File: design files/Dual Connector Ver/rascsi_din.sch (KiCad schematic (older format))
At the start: 24 parts, among them J1 Raspberry_Pi_2_3, J2 DB25_Female, J3 Conn_02x25_Odd_Even, U1 SN74LS641-1C, U2 SN74LS641-1C, U3 SN74LS641-1C, U4 SN74LS641-1C

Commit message: Corrected pinout to match original RaSCSI design.
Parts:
- removed D2, D3, D4, D5: LED_Small, LED_SMD:LED_0805_2012Metric, symbol Device:LED_Small
- removed FUSE1A1: R-US_0204_7, rascsi_din:0204_7, symbol rascsi_din-eagle-import:R-US_0204_7
- removed J1: Raspberry_Pi_2_3, Connector_PinSocket_2.54mm:PinSocket_2x20_P2.54mm_Vertical, symbol Connector:Raspberry_Pi_2_3
- removed J2: DB25_Female, Connector_Dsub:DSUB-25_Female_Horizontal_P2.77x2.84mm_EdgePinOffset4.94mm_Housed_MountingHolesOffset7.48mm, symbol Connector:DB25_Female
- removed J3: Conn_02x25_Odd_Even, Connector_PinHeader_2.54mm:PinHeader_2x25_P2.54mm_Vertical_SMD, symbol Connector_Generic:Conn_02x25_Odd_Even
- removed R1, R2, R3, R4: 10k, Resistor_SMD:R_0805_2012Metric, symbol Device:R_Small
- removed RN1, RN2: 10k, Resistor_THT:R_Array_SIP10, symbol Device:R_Network09
- removed RN3, RN5: 220, Resistor_THT:R_Array_SIP10, symbol Device:R_Network09
- removed RN4, RN6: 330, Resistor_THT:R_Array_SIP10, symbol Device:R_Network09
- added FUSE1A: R-US_0204_7, rascsi_din:0204_7, symbol rascsi_din-eagle-import:R-US_0204_7
- added JP1: PINHD-1X2, rascsi_din:1X02, symbol rascsi_din-eagle-import:PINHD-1X2
- added RN1, RN2: 10k, rascsi_din:RN-10, symbol rascsi_din-eagle-import:RN09
- added RN3, RN5: 220, rascsi_din:RN-10, symbol rascsi_din-eagle-import:RN09
- added RN4, RN6: 330, rascsi_din:RN-10, symbol rascsi_din-eagle-import:RN09
- added U$1: ZERO, rascsi_din:ZERO, symbol rascsi_din-eagle-import:ZERO
- added X1: F25?SHP, rascsi_din:F25HP, symbol rascsi_din-eagle-import:F25?SHP
- renumbered U$1 to U$2, U3 to U11, U4 to U22, U1 to U33, U2 to U44
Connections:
- net labels added: ACK, ATN, BSY, C-CD, C-IO, CD, D0, D1, D2, D3, D4, D5, D6, D7, DP, IO, MSG, REQ, RST, SEL
- net labels removed: C-C_D, C-I_O, DBG_LED, PI-ACK, PI-ATN, PI-BSY, PI-C_D, PI-D0, PI-D1, PI-D2, PI-D3, PI-D4, PI-D5, PI-D6, PI-D7, PI-DP, PI-I_O, PI-MSG, PI-REQ, PI-RST, PI-SEL
- wire segments 163 -> 417
- no-connect marks 11 -> 0
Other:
- note added: "3 4 etc"
- note added: "Goes 1 2"
- note added: "Note the original has ATOB for DIR for some reason...\nAnd G is active low, but this is taken care of in the design"
- note removed: "Activity, Debug and Power LEDs"
- note removed: "Change direction based upon PI-I_O"
- note removed: "DB-25 SCSI Connector"
- note removed: "DIR = +5v\nA is input, B is output"
- note removed: "DIR = GND\nB is input, A is output"
- note removed: "Note the original RaSCSI design calls the DIR pin "ATOB"\nEnable Input ("G") is active low, so always grounded."
- note removed: "ONLY THE DB-25 OR RIBBON CABLE SHOULD BE USED!!\nDO NOT USE BOTH AT THE SAME TIME!"
- note removed: "Pull-up resistors for Raspberry Pi 3.3v Signals"
- note removed: "Raspberry Pi Connector"
- note removed: "SCSI Bus Transceivers"
- note removed: "SCSI Ribbon Cable"
- note removed: "SCSI Termination Resistors"
- note removed: "Terminating Resistor Power"
- note removed: "This card include bus transceiver logic to allow a Raspberry \nPi to connect to a vintage Macintosh SCSI port. (It may \nwork with other systems as well)\n\nThis design is based upon fran-cap's design\nhttps://github.com/fran-cap/RASCSI-68kmlaver\n... which was based on the original Gimmons design:\nhttp://retropc.net/gimons/rascsi/\n\nThank you to everyone who has worked on this project!!"
- note removed: "fran-cap's Logo"

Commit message: Restored the correct version of the schematic & added notes to fix the PI-ACT signal. Also adding the gerber files.
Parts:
- removed FUSE1A: R-US_0204_7, rascsi_din:0204_7, symbol rascsi_din-eagle-import:R-US_0204_7
- removed JP1: PINHD-1X2, rascsi_din:1X02, symbol rascsi_din-eagle-import:PINHD-1X2
- removed RN1, RN2: 10k, rascsi_din:RN-10, symbol rascsi_din-eagle-import:RN09
- removed RN3, RN5: 220, rascsi_din:RN-10, symbol rascsi_din-eagle-import:RN09
- removed RN4, RN6: 330, rascsi_din:RN-10, symbol rascsi_din-eagle-import:RN09
- removed U$1: ZERO, rascsi_din:ZERO, symbol rascsi_din-eagle-import:ZERO
- removed X1: F25?SHP, rascsi_din:F25HP, symbol rascsi_din-eagle-import:F25?SHP
- added D2, D3, D4, D5: LED_Small, LED_SMD:LED_0805_2012Metric, symbol Device:LED_Small
- added FUSE1A1: R-US_0204_7, rascsi_din:0204_7, symbol rascsi_din-eagle-import:R-US_0204_7
- added H1: Hole1, MountingHole:MountingHole_2.7mm_M2.5_Pad_Via, symbol Mechanical:MountingHole_Pad
- added H2: Hole2, MountingHole:MountingHole_2.7mm_M2.5_Pad_Via, symbol Mechanical:MountingHole_Pad
- added H3: Hole3, MountingHole:MountingHole_2.7mm_M2.5_Pad_Via, symbol Mechanical:MountingHole_Pad
- added H4: Hole5, MountingHole:MountingHole_2.7mm_M2.5_Pad_Via, symbol Mechanical:MountingHole_Pad
- added H5: Hole4, MountingHole:MountingHole_2.7mm_M2.5_Pad_Via, symbol Mechanical:MountingHole_Pad
- added H6: Hole6, MountingHole:MountingHole_2.7mm_M2.5_Pad_Via, symbol Mechanical:MountingHole_Pad
- added J1: Raspberry_Pi_2_3, Connector_PinSocket_2.54mm:PinSocket_2x20_P2.54mm_Vertical, symbol Connector:Raspberry_Pi_2_3
- added J2: DLS3XS6AK44X, DLS3XS6AK44X, symbol Library_Loader_Parts:DLS3XS6AK44X
- added J3: Conn_02x25_Odd_Even, Connector_PinHeader_2.54mm:PinHeader_2x25_P2.54mm_Vertical_SMD, symbol Connector_Generic:Conn_02x25_Odd_Even
- added J4: I2C Pinout, Connector_PinSocket_2.54mm:PinSocket_1x05_P2.54mm_Vertical, symbol Connector:Conn_01x05_Male
- added JP1: Term_Enable_GND, Connector_PinSocket_2.54mm:PinSocket_1x02_P2.54mm_Vertical, symbol Device:Jumper_NC_Small
- added JP2: Term_Enable_5v, Connector_PinSocket_2.54mm:PinSocket_1x02_P2.54mm_Vertical, symbol Device:Jumper_NC_Small
- added L1: Mac, rascsi_din:mac_happy_small, symbol rascsi_din-eagle-import:LOGO
- added L2: Dogcow, rascsi_din:dogcow, symbol rascsi_din-eagle-import:LOGO
- added L3: Mac2, rascsi_din:mac_happy_small, symbol rascsi_din-eagle-import:LOGO
- added L4: Dogcow2, rascsi_din:dogcow, symbol rascsi_din-eagle-import:LOGO
- added L5, L7: Raspberry Pi, rascsi_din:pi_logo, symbol rascsi_din-eagle-import:LOGO
- added L6: Mac Trashcan, rascsi_din:mac_trashcan, symbol rascsi_din-eagle-import:LOGO
- added R1, R2, R4: 44, Resistor_SMD:R_0805_2012Metric, symbol Device:R_Small
- added R3: 112, Resistor_SMD:R_0805_2012Metric, symbol Device:R_Small
- added RN1, RN2: 10k, Resistor_THT:R_Array_SIP10, symbol Device:R_Network09
- added RN3, RN5: 220, Resistor_THT:R_Array_SIP10, symbol Device:R_Network09
- added RN4, RN6: 330, Resistor_THT:R_Array_SIP10, symbol Device:R_Network09
- renumbered U$2 to U$1, U33 to U1, U44 to U2, U11 to U3, U22 to U4
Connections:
- net labels added: C-C_D, C-I_O, DBG_LED, PI-ACK, PI-ATN, PI-BSY, PI-C_D, PI-D0, PI-D1, PI-D2, PI-D3, PI-D4, PI-D5, PI-D6, PI-D7, PI-DP, PI-I_O, PI-MSG, PI-REQ, PI-RST, PI-SEL, PI_SCL, PI_SDA
- net labels removed: ACK, ATN, BSY, C-CD, C-IO, CD, D0, D1, D2, D3, D4, D5, D6, D7, DP, IO, MSG, REQ, RST, SEL
- wire segments 417 -> 167
- no-connect marks 0 -> 9
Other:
- note added: "Activity, Debug and Power LEDs"
- note added: "Change direction based upon PI-I_O"
- note added: "DB-25 SCSI Connector"
- note added: "DIR = +5v\nA is input, B is output"
- note added: "DIR = GND\nB is input, A is output"
- note added: "Images"
- note added: "Jumper to enable or\ndisable SCSI \ntermination"
- note added: "Mounting Holes"
- note added: "Note the original RaSCSI design calls the DIR pin "ATOB"\nEnable Input ("G") is active low, so always grounded."
- note added: "ONLY THE DB-25 OR RIBBON CABLE SHOULD BE USED!!\nDO NOT USE BOTH AT THE SAME TIME!"
- note added: "Pull-up resistors for Raspberry Pi 3.3v Signals"
- note added: "Raspberry Pi Connector"
- note added: "SCSI Bus Transceivers"
- note added: "SCSI Ribbon Cable"
- note added: "SCSI Termination Resistors"
- note added: "THIS IS AN ERROR!!!\n"
- note added: "Terminating Resistor Power"
- note added: "This card include bus transceiver logic to allow a Raspberry \nPi to connect to a vintage Macintosh SCSI port. (It may \nwork with other systems as well)\n\nThis design is based upon fran-cap's design\nhttps://github.com/fran-cap/RASCSI-68kmlaver\n... which was based on the original Gimmons design:\nhttp://retropc.net/gimons/rascsi/\n\nThank you to everyone who has worked on this project!!"
- note added: "This should be PI-ACT. To correct this, cut \nthe trace to pin 1 of U3, and run a jumper \nwire to Pin 7 of the Raspberry Pi GPIO header."
- note removed: "3 4 etc"
- note removed: "Goes 1 2"
- note removed: "Note the original has ATOB for DIR for some reason...\nAnd G is active low, but this is taken care of in the design"

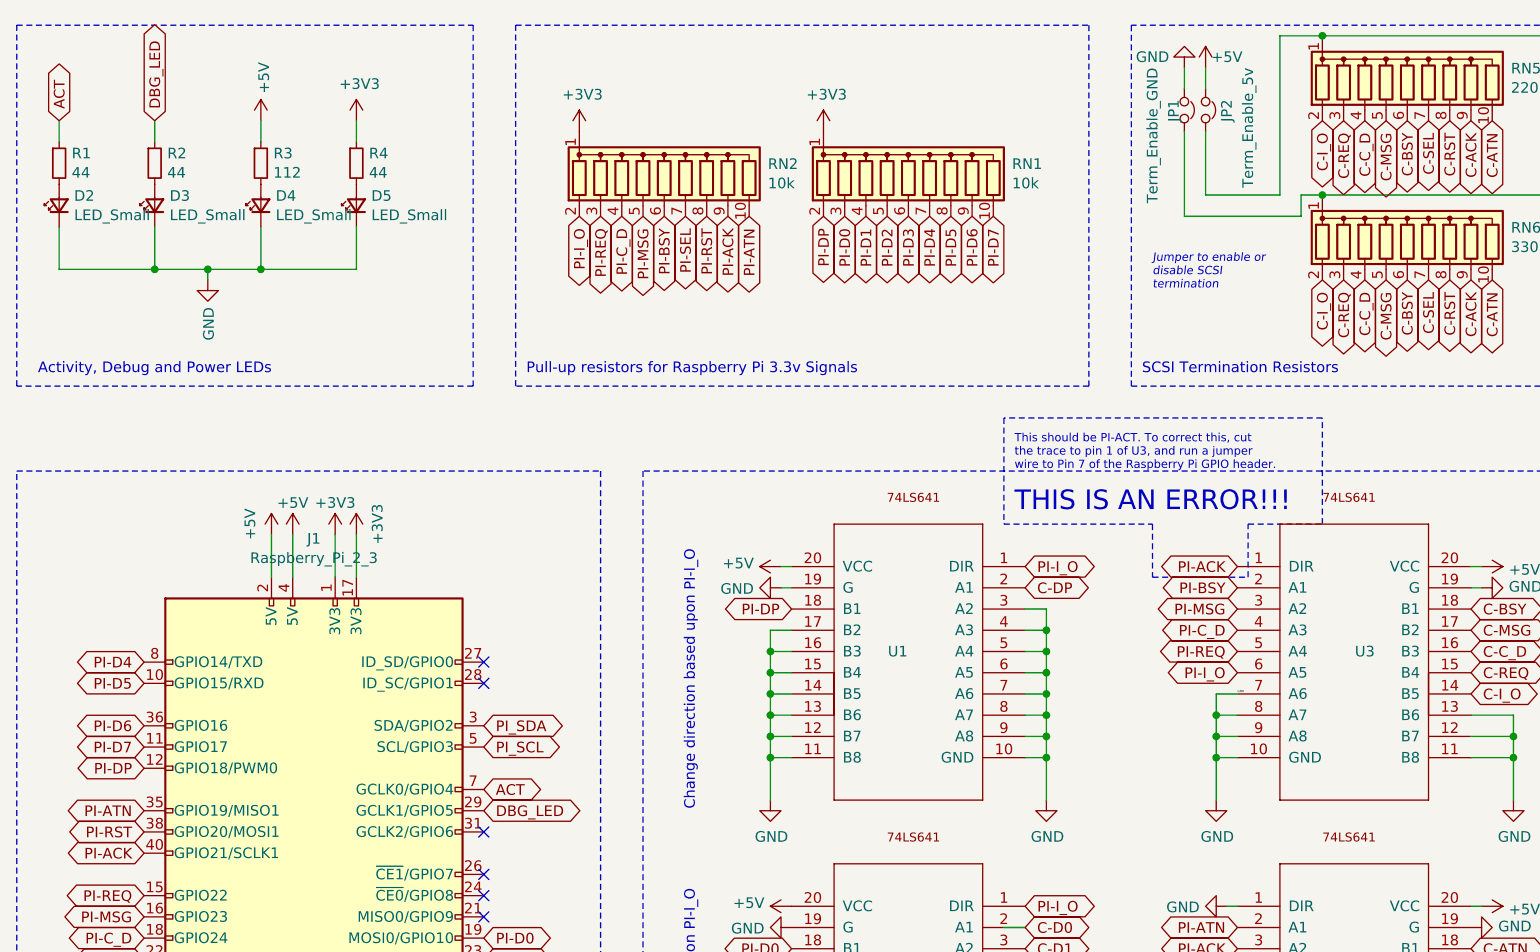
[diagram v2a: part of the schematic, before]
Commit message: Corrected ACT signal line
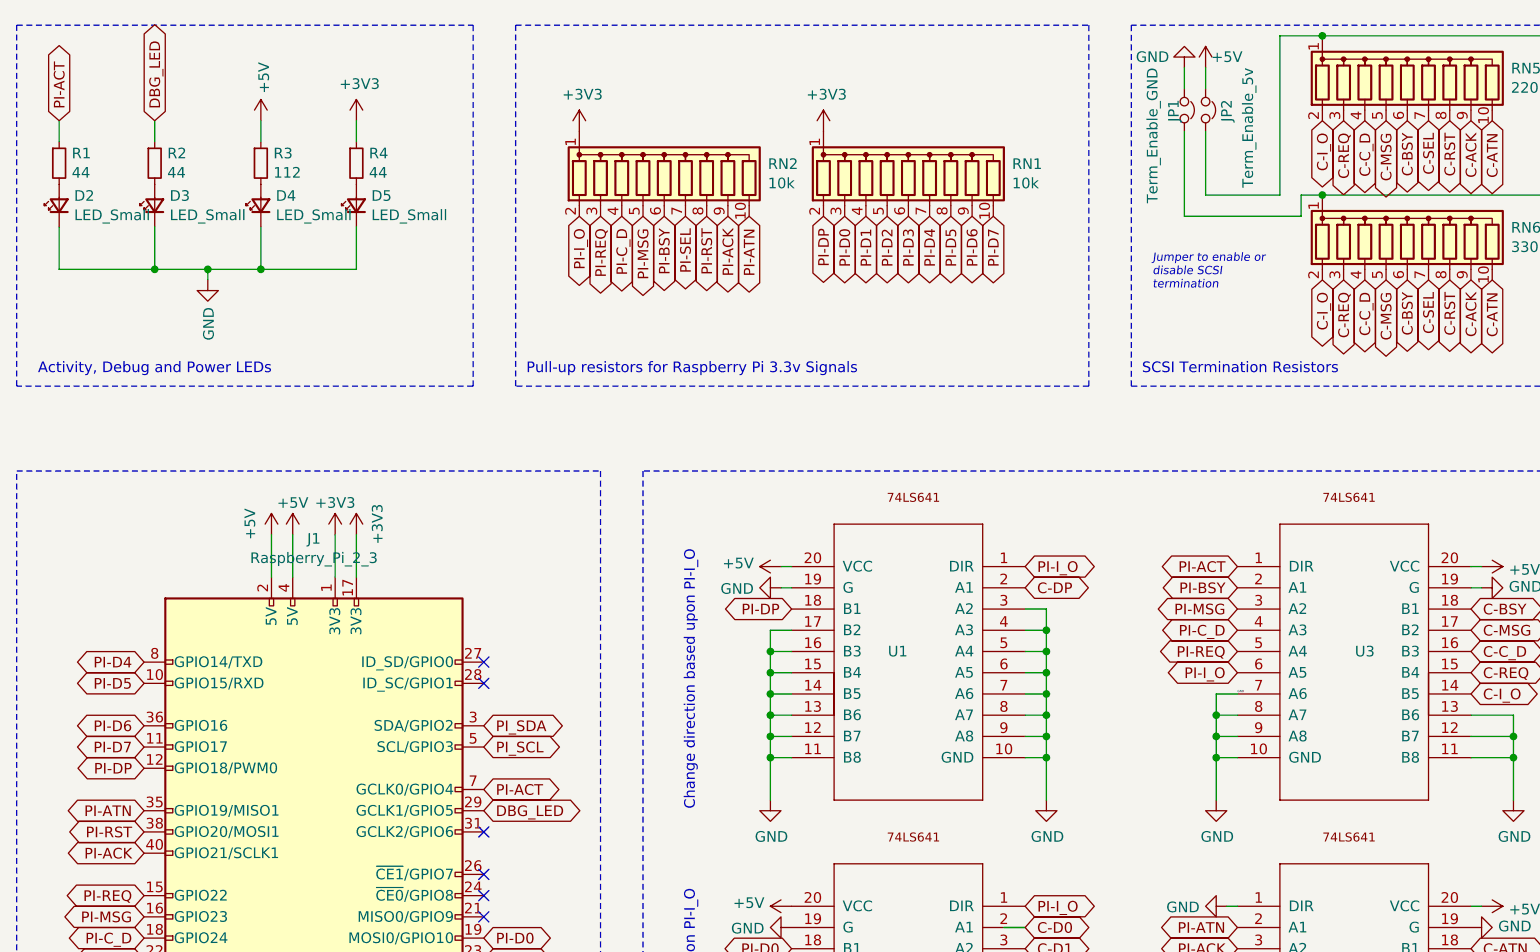
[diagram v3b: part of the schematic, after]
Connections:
- net labels added: PI-ACT
- net labels removed: ACT
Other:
- note removed: "THIS IS AN ERROR!!!\n"
- note removed: "This should be PI-ACT. To correct this, cut \nthe trace to pin 1 of U3, and run a jumper \nwire to Pin 7 of the Raspberry Pi GPIO header."
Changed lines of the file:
@@
-$EndComp
-$Comp
-L power:+5V #PWR028
-U 1 1 6072B611
-P 6150 750
-F 0 "#PWR028" H 6150 600 50  0001 C CNN
-F 1 "+5V" H 6250 800 50  0000 C CNN
-F 2 "" H 6150 750 50  0001 C CNN
-F 3 "" H 6150 750 50  0001 C CNN
-	1    6150 750
-	1    0    0    -1
 $EndComp
 $Comp
@@
 	1    7100 1550
 	1    0    0    -1
-$EndComp
-$Comp
-L power:GND #PWR026
-U 1 1 6072B62D
-P 6050 750
-F 0 "#PWR026" H 6050 500 50  0001 C CNN
-F 1 "GND" H 6200 700 50  0000 C CNN
-F 2 "" H 6050 750 50  0001 C CNN
-F 3 "" H 6050 750 50  0001 C CNN
-	1    6050 750
-	-1   0    0    1
 $EndComp
 Text GLabel 7400 3600 2    50   BiDi ~ 0
@@
 PI-ATN
 Text GLabel 6300 3100 0    50   BiDi ~ 0
-PI-ACK
+PI-ACT
 Text GLabel 6300 5000 0    50   BiDi ~ 0
 PI-RST
@@
 PI-DP
 Text GLabel 750  1000 1    50   BiDi ~ 0
-ACT
+PI-ACT
 $Comp
 L power:GND #PWR08
@@
 PI-SEL
 Text GLabel 2750 4150 2    50   BiDi ~ 0
-ACT
+PI-ACT
 $Comp
 L power:+5V #PWR01
@@
 $EndComp
 Connection ~ 3300 7600
-$Comp
-L Library_Loader_Parts:DLS3XS6AK44X J2
-U 1 1 5F429403
-P 9200 4650
-F 0 "J2" H 11044 4696 50  0000 L CNN
-F 1 "DLS3XS6AK44X" V 10850 3950 50  0000 L CNN
-F 2 "DLS3XS6AK44X" H 10850 4950 50  0001 L CNN
-F 3 "https://componentsearchengine.com/Datasheets/1/DLS3XS6AK44X.pdf" H 10850 4850 50  0001 L CNN
-F 4 "D-Sub Standard Connectors 25P F R/A .370 4-40 C/W HEX" H 10850 4750 50  0001 L CNN "Description"
-F 5 "12.5" H 10850 4650 50  0001 L CNN "Height"
-F 6 "706-DLS3XS6AK44X" H 10850 4550 50  0001 L CNN "Mouser Part Number"
-F 7 "https://www.mouser.com/Search/Refine.aspx?Keyword=706-DLS3XS6AK44X" H 10850 4450 50  0001 L CNN "Mouser Price/Stock"
-F 8 "CONEC" H 10850 4350 50  0001 L CNN "Manufacturer_Name"
-F 9 "DLS3XS6AK44X" H 10850 4250 50  0001 L CNN "Manufacturer_Part_Number"
-	1    9200 4650
-	0    -1   -1   0
-$EndComp
 Text GLabel 8700 3850 0    50   BiDi ~ 0
 C-D0
@@
 Mounting Holes
 $Comp
-L power:+5V #PWR048
-U 1 1 5F0B94FB
-P 2950 6250
-F 0 "#PWR048" H 2950 6100 50  0001 C CNN
-F 1 "+5V" V 2950 6450 50  0000 C CNN
-F 2 "" H 2950 6250 50  0001 C CNN
-F 3 "" H 2950 6250 50  0001 C CNN
-	1    2950 6250
-	0    -1   -1   0
-$EndComp
-$Comp
 L power:GND #PWR047
 U 1 1 5F0B9E0E
@@
 Text GLabel 2950 5950 0    50   BiDi ~ 0
 PI_SCL
+Wire Notes Line
+	3300 5700 2550 5700
+Wire Notes Line
+	2550 5700 2550 6400
+NoConn ~ 2750 4750
+NoConn ~ 2750 4650
+NoConn ~ 2750 4550
+NoConn ~ 2750 4350
+NoConn ~ 2750 3550
+NoConn ~ 2750 3650
+Wire Notes Line
+	5800 2250 8900 2250
+Wire Wire Line
+	6700 600  7800 600
+Connection ~ 6700 600
+Wire Wire Line
+	6600 1350 6700 1350
+Wire Wire Line
+	7800 1350 6700 1350
+Connection ~ 6700 1350
+$Comp
+L rascsi_din-eagle-import:LOGO L7
+U 1 1 5F2D2B3B
+P 9050 6300
+F 0 "L7" H 8900 6300 50  0000 R CNN
+F 1 "Raspberry Pi" H 8950 6350 50  0000 R CNN
+F 2 "rascsi_din:pi_logo" H 9050 6300 50  0001 C CNN
+F 3 "" H 9050 6300 50  0001 C CNN
+	1    9050 6300
+	-1   0    0    1
+$EndComp
+$Comp
+L rascsi_din-eagle-import:LOGO L5
+U 1 1 5EFCDD94
+P 9550 5950
+F 0 "L5" H 9350 5950 50  0000 R CNN
+F 1 "Raspberry Pi" H 9400 6000 50  0000 R CNN
+F 2 "rascsi_din:pi_logo" H 9550 5950 50  0001 C CNN
+F 3 "" H 9550 5950 50  0001 C CNN
+	1    9550 5950
+	-1   0    0    1
+$EndComp
+$Comp
+L power:+5V #PWR048
+U 1 1 5F0B94FB
+P 2950 6250
+F 0 "#PWR048" H 2950 6100 50  0001 C CNN
+F 1 "+5V" V 2950 6450 50  0000 C CNN
+F 2 "" H 2950 6250 50  0001 C CNN
+F 3 "" H 2950 6250 50  0001 C CNN
+	1    2950 6250
+	0    -1   -1   0
+$EndComp
 $Comp
 L Connector:Conn_01x05_Male J4
@@
 	-1   0    0    1
 $EndComp
-Wire Notes Line
-	3300 5700 2550 5700
-Wire Notes Line
-	2550 5700 2550 6400
-NoConn ~ 2750 4750
-NoConn ~ 2750 4650
-NoConn ~ 2750 4550
-NoConn ~ 2750 4350
-NoConn ~ 2750 3550
-NoConn ~ 2750 3650
-Wire Notes Line
-	5800 2250 8900 2250
-Wire Wire Line
-	6150 1350 6500 1350
-Wire Wire Line
-	6500 1350 6500 600
+$Comp
+L Library_Loader_Parts:DLS3XS6AK44X J2
+U 1 1 5F429403
+P 9200 4650
+F 0 "J2" H 11044 4696 50  0000 L CNN
+F 1 "DLS3XS6AK44X" V 10850 3950 50  0000 L CNN
+F 2 "DLS3XS6AK44X" H 10850 4950 50  0001 L CNN
+F 3 "https://componentsearchengine.com/Datasheets/1/DLS3XS6AK44X.pdf" H 10850 4850 50  0001 L CNN
+F 4 "D-Sub Standard Connectors 25P F R/A .370 4-40 C/W HEX" H 10850 4750 50  0001 L CNN "Description"
+F 5 "12.5" H 10850 4650 50  0001 L CNN "Height"
+F 6 "706-DLS3XS6AK44X" H 10850 4550 50  0001 L CNN "Mouser Part Number"
+F 7 "https://www.mouser.com/Search/Refine.aspx?Keyword=706-DLS3XS6AK44X" H 10850 4450 50  0001 L CNN "Mouser Price/Stock"
+F 8 "CONEC" H 10850 4350 50  0001 L CNN "Manufacturer_Name"
+F 9 "DLS3XS6AK44X" H 10850 4250 50  0001 L CNN "Manufacturer_Part_Number"
+	1    9200 4650
+	0    -1   -1   0
+$EndComp
+Wire Wire Line
+	6600 1450 6600 1350
 Wire Wire Line
 	6500 600  6700 600
 Wire Wire Line
-	6700 600  7800 600
-Connection ~ 6700 600
-Wire Wire Line
-	6050 1450 6600 1450
-Wire Wire Line
-	6600 1450 6600 1350
-Wire Wire Line
-	6600 1350 6700 1350
-Wire Wire Line
-	7800 1350 6700 1350
-Connection ~ 6700 1350
+	6150 850  6150 750
+Wire Wire Line
+	6050 850  6050 750
+$Comp
+L power:GND #PWR026
+U 1 1 6072B62D
+P 6050 750
+F 0 "#PWR026" H 6050 500 50  0001 C CNN
+F 1 "GND" H 6200 700 50  0000 C CNN
+F 2 "" H 6050 750 50  0001 C CNN
+F 3 "" H 6050 750 50  0001 C CNN
+	1    6050 750
+	-1   0    0    1
+$EndComp
+$Comp
+L power:+5V #PWR028
+U 1 1 6072B611
+P 6150 750
+F 0 "#PWR028" H 6150 600 50  0001 C CNN
+F 1 "+5V" H 6250 800 50  0000 C CNN
+F 2 "" H 6150 750 50  0001 C CNN
+F 3 "" H 6150 750 50  0001 C CNN
+	1    6150 750
+	1    0    0    -1
+$EndComp
 Text Notes 5900 1800 0    39   Italic 0
 Jumper to enable or\ndisable SCSI \ntermination
+Wire Wire Line
+	6500 1350 6500 600
+Wire Wire Line
+	6050 1450 6600 1450
+Wire Wire Line
+	6150 1350 6500 1350
+Wire Wire Line
+	6050 1050 6050 1450
+Wire Wire Line
+	6150 1050 6150 1350
 $Comp
 L Device:Jumper_NC_Small JP1
@@
 	0    1    1    0
 $EndComp
-Wire Wire Line
-	6050 850  6050 750
-Wire Wire Line
-	6150 850  6150 750
-Wire Wire Line
-	6150 1050 6150 1350
-Wire Wire Line
-	6050 1050 6050 1450
-$Comp
-L rascsi_din-eagle-import:LOGO L7
-U 1 1 5F2D2B3B
-P 9050 6300
-F 0 "L7" H 8900 6300 50  0000 R CNN
-F 1 "Raspberry Pi" H 8950 6350 50  0000 R CNN
-F 2 "rascsi_din:pi_logo" H 9050 6300 50  0001 C CNN
-F 3 "" H 9050 6300 50  0001 C CNN
-	1    9050 6300
-	-1   0    0    1
-$EndComp
-$Comp
-L rascsi_din-eagle-import:LOGO L5
-U 1 1 5EFCDD94
-P 9550 5950
-F 0 "L5" H 9350 5950 50  0000 R CNN
-F 1 "Raspberry Pi" H 9400 6000 50  0000 R CNN
-F 2 "rascsi_din:pi_logo" H 9550 5950 50  0001 C CNN
-F 3 "" H 9550 5950 50  0001 C CNN
-	1    9550 5950
-	-1   0    0    1
-$EndComp
-Text Notes 5250 2850 0    92   ~ 0
-THIS IS AN ERROR!!!\n
-Text Notes 5250 2650 0    39   ~ 0
-This should be PI-ACT. To correct this, cut \nthe trace to pin 1 of U3, and run a jumper \nwire to Pin 7 of the Raspberry Pi GPIO header.
-Wire Notes Line
-	5200 2400 5200 2900
-Wire Notes Line
-	5200 2900 5900 2900
-Wire Notes Line
-	5900 2900 5900 3150
-Wire Notes Line
-	5900 3150 6350 3150
-Wire Notes Line
-	6350 3150 6350 2900
-Wire Notes Line
-	6350 2900 6700 2900
-Wire Notes Line
-	6700 2900 6700 2400
-Wire Notes Line
-	6700 2400 5200 2400
 $EndSCHEMATC
